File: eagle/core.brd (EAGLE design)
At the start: 103.5 x 19.7 mm, 35 parts, among them T1 BC846, T2 BC846, T3 BC846, T4 BC846

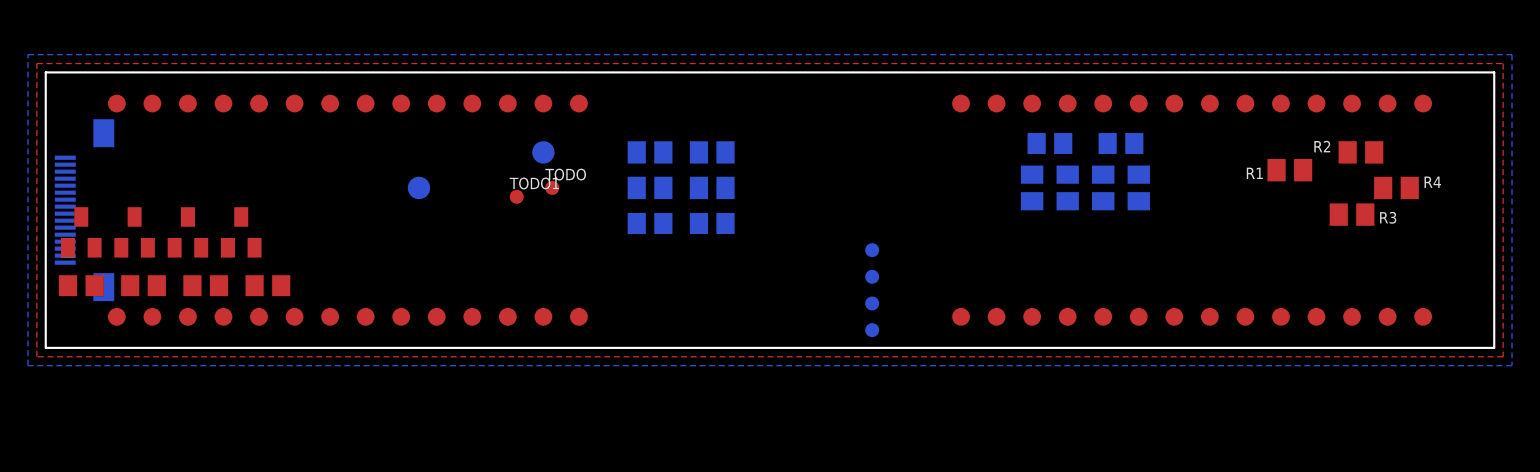
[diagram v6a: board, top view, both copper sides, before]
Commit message: core pcb improvements
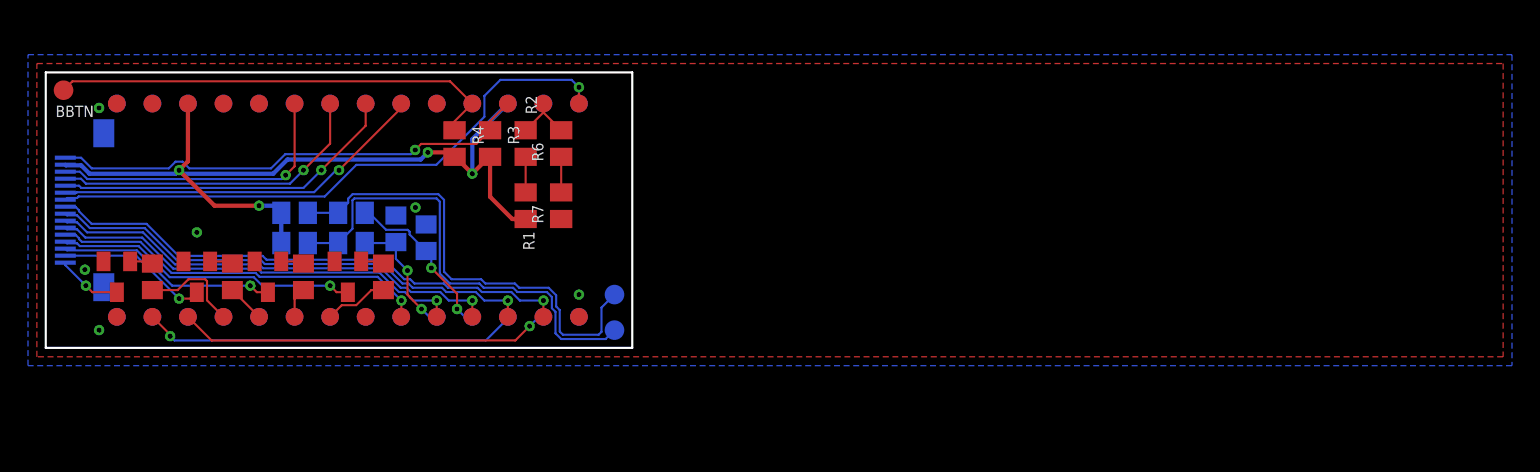
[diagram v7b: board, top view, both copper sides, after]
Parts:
- removed 3V, GND: TPTP16R, testpad:TP16R
- removed C3, C4: 10u, resistor:C0805
- removed MBTN, SBTN, TODO, TODO1: TPTP10R, testpad:TP10R
- removed R11, R12: 10k, resistor:M0805
- added BBTN: TPTP14R, testpad:TP14R
- ENCL, ENCR: value TPTP10R -> TPTP14R; device testpad:TP10R -> testpad:TP14R
- R6, R7: value 10k -> 20M
- moved R4 67.4 mm to (29.2, 14.6), turned to 270 degrees
- moved R3 61.8 mm to (31.8, 14.6), turned to 270 degrees
- moved R2 59.7 mm to (34.3, 14.6), turned to 270 degrees
- moved U$2 57.8 mm to (22.9, 9.84), flipped to the bottom
- moved R1 54.7 mm to (34.3, 10.2), turned to 270 degrees
- moved R6 36.3 mm to (36.8, 14.6), flipped to the top
- moved R7 33.7 mm to (36.8, 10.2), flipped to the top, turned to 90 degrees
- moved R8 30.2 mm to (17.8, 9.65)
- moved R9 26.2 mm to (17.8, 7.49), turned to 0 degrees
- moved R5 25.8 mm to (21.8, 9.65), turned to 0 degrees
- moved R10 21.7 mm to (21.8, 7.49)
- moved C1 20.5 mm to (27.2, 7.87), turned to 90 degrees
- moved ENCL 18.6 mm to (40.6, 3.81)
- moved ENCR 18.5 mm to (40.6, 1.27)
- moved C2 18.2 mm to (25.0, 8.51), turned to 90 degrees
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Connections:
- removed net ANTT1: R1.1, R2.2, U$1.14
- removed net ANTT2: R3.1, R4.2, U$1.15
- removed net MBTN: MBTN.TP, R11.1, R12.2
- removed net MBTNPIN: C4.1, R12.1, TODO.TP
- removed net SBTN: R6.1, R7.2, SBTN.TP
- removed net SBTNPIN: C3.1, R7.1, TODO1.TP
- new net ANTPIN: R2.1, R6.2, U$1.14
- new net BBTN: BBTN.TP, R4.1, U$1.16
- new net N$6: R6.1, R7.2
- new net N$7: R1.1, R2.2
- new net PBTN: R3.1, U$1.15, U$3.16
- net 3V: now also R4.2; no longer 3V.TP, R11.2, R6.2
- net ENCPINL: now also U$2.2
- net ENCPINR: now also U$2.3
- net GND: now also R7.1; no longer C3.2, C4.2, GND.TP, R2.1, R4.1, U$3.16
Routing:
- net 3V: track 0.00 -> 60.5 mm, vias 0 -> 4
- net SCK: track 0.00 -> 42.5 mm, vias 0 -> 1
- net MOSI: track 0.00 -> 38.1 mm, vias 0 -> 1
- net TFTCS: track 0.00 -> 35.4 mm, vias 0 -> 1
- net PBTN: track 0.00 -> 34.6 mm, vias 0 -> 1
- net ENCL: track 0.00 -> 33.4 mm
- net ENCR: track 0.00 -> 33.2 mm
- net DC: track 0.00 -> 32.6 mm, vias 0 -> 1
- net BBTN: track 0.00 -> 32.6 mm
- net DOUT: track 0.00 -> 29.9 mm, vias 0 -> 1
- net TFTRST: track 0.00 -> 27.2 mm, vias 0 -> 1
- net T4RX: track 0.00 -> 26.9 mm, vias 0 -> 1
- net T4TX: track 0.00 -> 26.9 mm, vias 0 -> 1
- net SDA: track 0.00 -> 26.8 mm, vias 0 -> 1
- net SCL: track 0.00 -> 25.0 mm, vias 0 -> 1
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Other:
- board size 103.5 x 19.7 mm -> 41.9 x 19.7 mm

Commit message: Added optional I2C pullups and started renderer.
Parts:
- added R11, R12: (no value), resistor:R0805
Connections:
- net 3V: now also R11.2, R12.2
- net SCL: now also R11.1
- net SDA: now also R12.1
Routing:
- net 3V: track 60.5 -> 63.1 mm
- net SDA: track 26.8 -> 28.0 mm
- net PWM2: track 2.70 -> 3.33 mm
- net SCL: track 25.0 -> 25.5 mm
